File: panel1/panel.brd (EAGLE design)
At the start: 50.1 x 50.4 mm, 33 parts, among them J1 AVR_SPI_PRG_62X3_LOCK, J3 AVR_SPI_PRG_62X3_LOCK

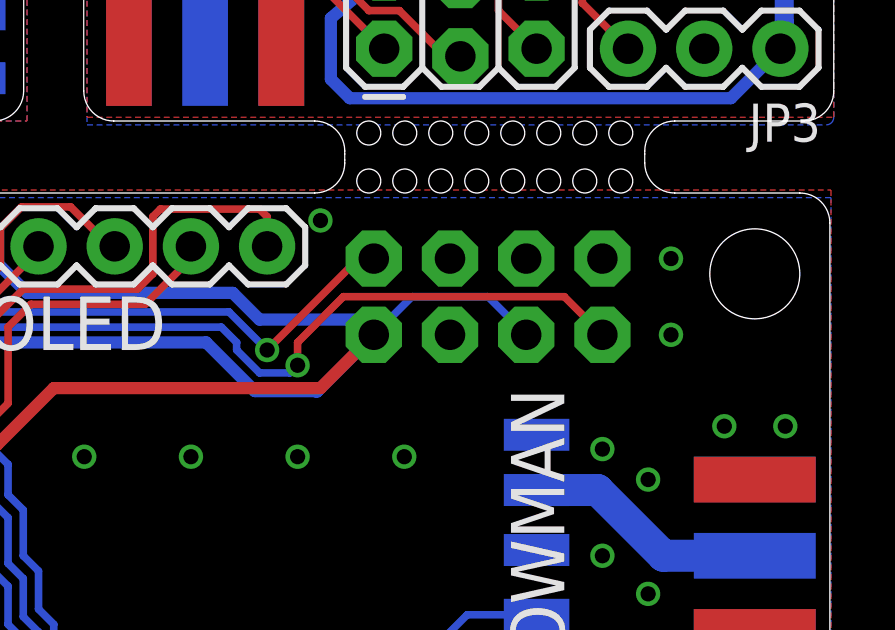
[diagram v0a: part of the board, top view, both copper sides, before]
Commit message: tied reset line high (in panelised only)
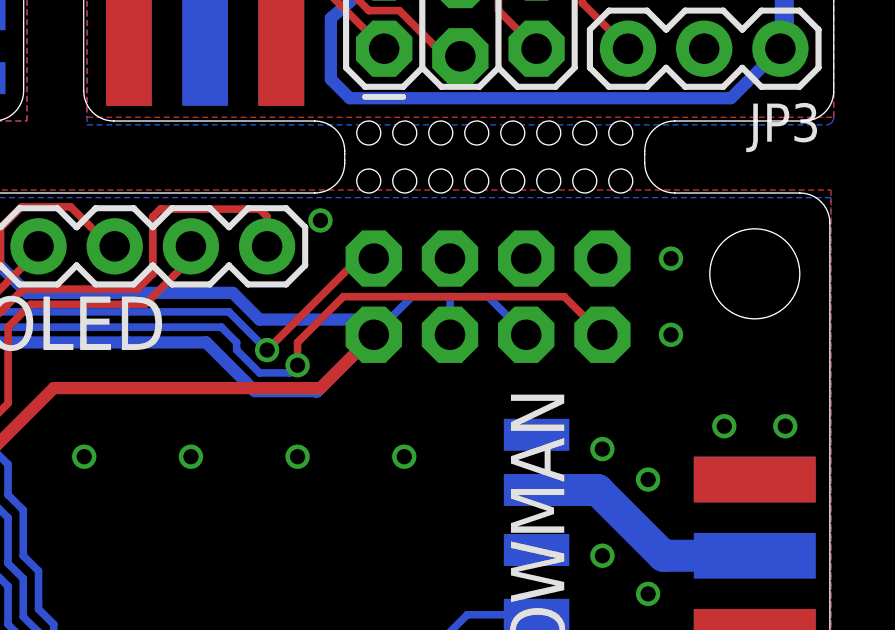
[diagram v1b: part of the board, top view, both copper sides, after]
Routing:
- net VCC3: track 115.0 -> 116.2 mm
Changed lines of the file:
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@@
 <setting verticaltext="up"/>
 </settings>
-<grid distance="0.1" unitdist="mm" unit="mm" style="lines" multiple="1" display="yes" altdistance="0.005" altunitdist="inch" altunit="inch"/>
+<grid distance="0.05" unitdist="inch" unit="inch" style="lines" multiple="1" display="yes" altdistance="0.005" altunitdist="inch" altunit="inch"/>
 <layers>
 <layer number="1" name="Top" color="4" fill="1" visible="yes" active="yes"/>
@@
 <wire x1="34.16" y1="19.382" x2="34.668" y2="18.874" width="0.4064" layer="16"/>
 <wire x1="34.668" y1="18.874" x2="35.938" y2="20.144" width="0.254" layer="16"/>
-<wire x1="35.938" y1="20.144" x2="38.478" y2="20.144" width="0.254" layer="16"/>
+<wire x1="35.938" y1="20.144" x2="37.211" y2="20.144" width="0.254" layer="16"/>
+<wire x1="37.211" y1="20.144" x2="38.478" y2="20.144" width="0.254" layer="16"/>
 <wire x1="38.478" y1="20.144" x2="39.748" y2="18.874" width="0.254" layer="16"/>
 <wire x1="32.79" y1="16.996" x2="30.704" y2="16.996" width="0.4064" layer="16"/>
@@
 <wire x1="32.636" y1="17.096" x2="32.89" y2="17.096" width="0.4064" layer="1"/>
 <wire x1="32.89" y1="17.096" x2="34.668" y2="18.874" width="0.4064" layer="1"/>
+<wire x1="37.211" y1="18.923" x2="37.211" y2="19.431" width="0.254" layer="16"/>
+<wire x1="37.211" y1="19.431" x2="37.211" y2="20.144" width="0.254" layer="16"/>
 </signal>
 <signal name="SWDAT1">
